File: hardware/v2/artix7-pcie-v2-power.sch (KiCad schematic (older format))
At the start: 45 parts, among them U3 LP5907MFX, X1 APXS006A0X4-SRZ, X2 APXS006A0X4-SRZ, X3 APXS006A0X4-SRZ, X4 APXS006A0X4-SRZ

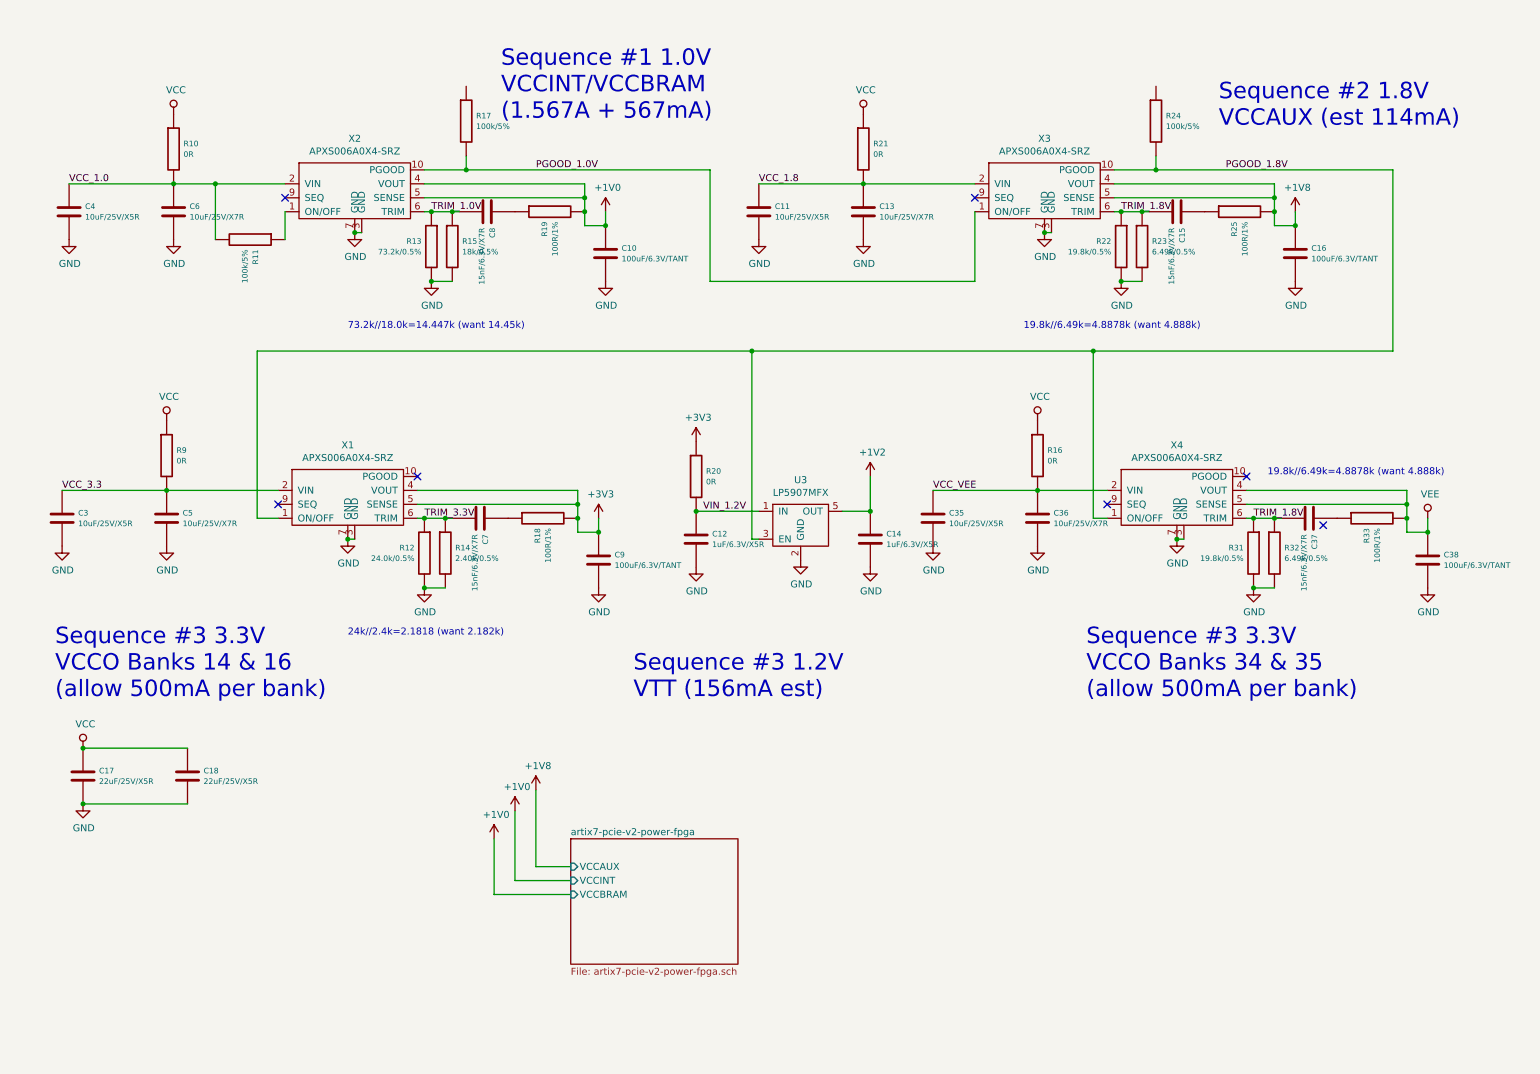
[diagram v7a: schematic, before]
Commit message: v2 pcb/schematic update : drc passing, need to add caps
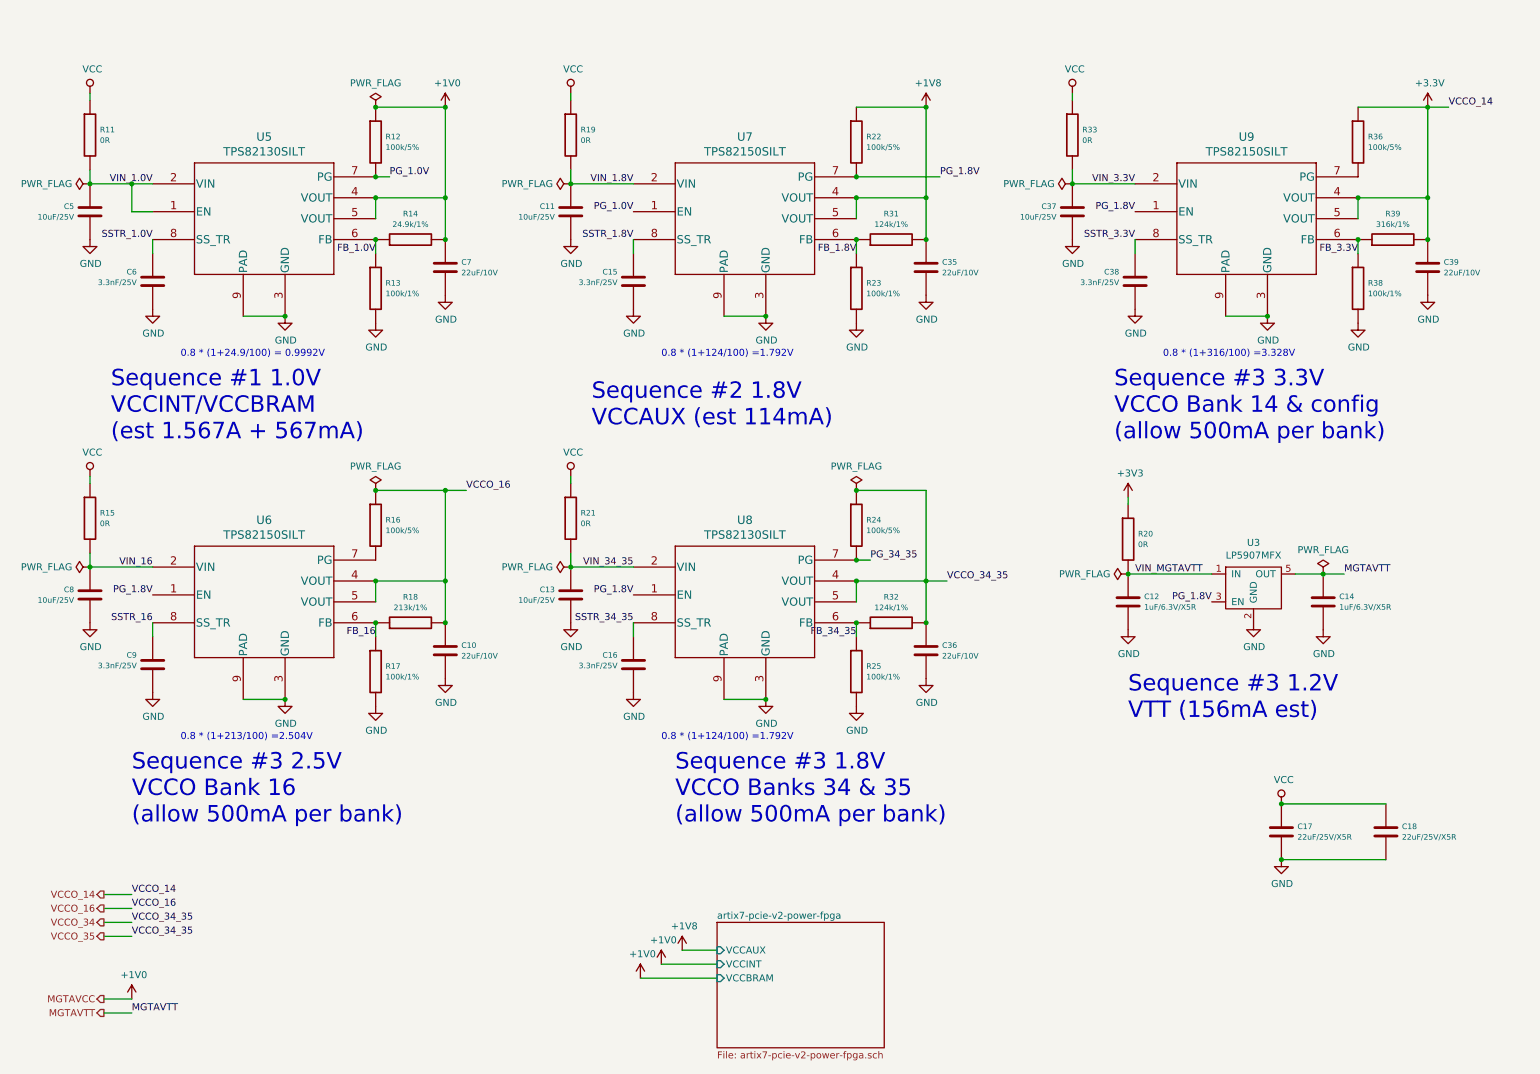
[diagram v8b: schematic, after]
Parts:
- removed C3, C4: 10uF/25V/X5R, tom-passives:C_0603_1608Metric_Pad1.05x0.95mm_HandSolder, symbol tom-passives:C
- removed R10, R9: 0R, tom-passives:C_0603_1608Metric, symbol tom-passives:R
- removed X1, X2, X3, X4: APXS006A0X4-SRZ, tom-modules:APXS006, symbol tom-modules:APXS006A0X4-SRZ
- added C39: 22uF/10V, tom-passives:C_0805_2012Metric, symbol tom-passives:C
- added R36: 100k/5%, tom-passives:C_0402_1005Metric, symbol tom-passives:R
- added R38: 100k/1%, tom-passives:C_0402_1005Metric, symbol tom-passives:R
- added R39: 316k/1%, tom-passives:C_0402_1005Metric, symbol tom-passives:R
- added U5, U8: TPS82130SILT, tom-modules:TPS82130SILT, symbol tom-modules:TPS821x0SILT
- added U6, U7, U9: TPS82150SILT, tom-modules:TPS82130SILT, symbol tom-modules:TPS821x0SILT
- C10: value 100uF/6.3V/TANT -> 22uF/10V; footprint tom-passives:C_0402_1005Metric -> tom-passives:C_0805_2012Metric; Digikey 478-9393-1-ND -> (none); MFGPN (none) -> C2012X7S1A226M125AC
- C11: value 10uF/25V/X5R -> 10uF/25V; footprint tom-passives:C_0603_1608Metric_Pad1.05x0.95mm_HandSolder -> tom-passives:C_1206_3216Metric; MFGPN (none) -> C3216X7R1E106M160AE
- C13, C5: value 10uF/25V/X7R -> 10uF/25V; footprint tom-passives:C_0603_1608Metric_Pad1.05x0.95mm_HandSolder -> tom-passives:C_1206_3216Metric; MFGPN (none) -> C3216X7R1E106M160AE
- C15: value 15nF/6.3V/X7R -> 3.3nF/25V
- C16, C38, C9: value 100uF/6.3V/TANT -> 3.3nF/25V; Digikey 478-9393-1-ND -> (none)
- C35: value 10uF/25V/X5R -> 22uF/10V; footprint tom-passives:C_0603_1608Metric_Pad1.05x0.95mm_HandSolder -> tom-passives:C_0805_2012Metric; MFGPN (none) -> C2012X7S1A226M125AC
- C36: value 10uF/25V/X7R -> 22uF/10V; footprint tom-passives:C_0603_1608Metric_Pad1.05x0.95mm_HandSolder -> tom-passives:C_0805_2012Metric; MFGPN (none) -> C2012X7S1A226M125AC
- C37, C8: value 15nF/6.3V/X7R -> 10uF/25V; footprint tom-passives:C_0402_1005Metric -> tom-passives:C_1206_3216Metric; MFGPN (none) -> C3216X7R1E106M160AE
- C6: value 10uF/25V/X7R -> 3.3nF/25V; footprint tom-passives:C_0603_1608Metric_Pad1.05x0.95mm_HandSolder -> tom-passives:C_0402_1005Metric
- C7: value 15nF/6.3V/X7R -> 22uF/10V; footprint tom-passives:C_0402_1005Metric -> tom-passives:C_0805_2012Metric; MFGPN (none) -> C2012X7S1A226M125AC
- R11: value 100k/5% -> 0R; footprint tom-passives:C_0402_1005Metric -> tom-passives:R_0603_1608Metric
- R12: value 24.0k/0.5% -> 100k/5%
- R13: value 73.2k/0.5% -> 100k/1%
- R14: value 2.40k/0.5% -> 24.9k/1%
- R15: value 18k/0.5% -> 0R; footprint tom-passives:C_0402_1005Metric -> tom-passives:R_0603_1608Metric
- R16: value 0R -> 100k/5%; footprint tom-passives:C_0603_1608Metric -> tom-passives:C_0402_1005Metric
- R17: value 100k/5% -> 100k/1%
- R18: value 100R/1% -> 213k/1%
- R19, R33: value 100R/1% -> 0R; footprint tom-passives:C_0402_1005Metric -> tom-passives:R_0603_1608Metric
- R21: footprint tom-passives:C_0402_1005Metric -> tom-passives:R_0603_1608Metric
- R22: value 19.8k/0.5% -> 100k/5%
- R23: value 6.49k/0.5% -> 100k/1%
- R25: value 100R/1% -> 100k/1%
- R31: value 19.8k/0.5% -> 124k/1%
- R32: value 6.49k/0.5% -> 124k/1%
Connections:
- net PGOOD_1.0V is gone; now on net GND: R17.2
- net VCC_3.3 is gone; now on net GND: C5.1
- net +1V0: now also C7.1, R12.1, R14.2, U5.4 (VOUT), U5.5 (VOUT); no longer C10.1, R19.2
- net +1V8: now also C35.1, R22.1, R31.2, U7.4 (VOUT), U7.5 (VOUT); no longer C16.1, R25.2
- net +3V3: now also C39.1, R36.1, R39.2, U9.4 (VOUT), U9.5 (VOUT); no longer C9.1, R18.2
- net GND: now also C11.1, C13.1, C15.1, C16.1, C37.1, C38.1, C6.1, C7.2, C8.1, C9.1, R25.2, C39.2, R38.2, U5.3 (GND), U5.9 (PAD), U6.3 (GND), U6.9 (PAD), U7.3 (GND), U7.9 (PAD), U8.3 (GND), U8.9 (PAD), U9.3 (GND), U9.9 (PAD); no longer C11.2, C13.2, C16.2, C38.2, C5.2, C6.2, C9.2, R12.2, R14.2, R15.2, R22.2, R31.2, R32.2
- net VCC: now also R11.1, R15.1, R19.1, R33.1; no longer R16.1
- net FB_16: now reaches R17.1
- net FB_16: now also R18.1, U6.6 (FB)
- net VCCO_34: now reaches R24.1
- net VCCO_34: now also C36.1, R32.2, U8.4 (VOUT), U8.5 (VOUT)
- net FB_34_35: now reaches R25.1
- net FB_34_35: now also R32.1, U8.6 (FB); no longer C15.1
- net +1V2 renamed MGTAVTT
- net PGOOD_1.8V renamed PG_1.8V
- net PG_1.8V: now also R22.2, U6.1 (EN), U7.7 (PG), U8.1 (EN), U9.1 (EN); no longer R24.2
- removed net TRIM_1.0V: C8.2, R13.1, R15.1
- removed net TRIM_1.8V: C15.2, C37.2, R22.1, R23.1, R31.1, R32.1
- removed net TRIM_3.3V: C7.2, R12.1, R14.1
- net VCC_1.0 renamed VIN_1.0V
- net VIN_1.0V: now also C5.2, U5.1 (EN), U5.2 (VIN); no longer C6.1
- removed net VCC_1.8: C11.1, C13.1, R21.2
- removed net VCC_VEE: C35.1, C36.1, R16.2
- net VEE renamed VIN_3.3V
- net VIN_3.3V: now also C37.2, U9.2 (VIN); no longer C38.1
- net VIN_1.2V renamed VIN_MGTAVTT
- new net: R36.2, U9.7 (PG)
- new net: R16.2, U6.7 (PG)
- new net FB_1.0V: R13.1, R14.1, U5.6 (FB)
- new net FB_1.8V: R23.1, R31.1, U7.6 (FB)
- new net FB_3.3V: R38.1, R39.1, U9.6 (FB)
- new net PG_1.0V: R12.2, U5.7 (PG), U7.1 (EN)
- new net PG_34_35: R24.2, U8.7 (PG)
- new net SSTR_1.0V: C6.2, U5.8 (SS_TR)
- new net SSTR_1.8V: C15.2, U7.8 (SS_TR)
- new net SSTR_16: C9.2, U6.8 (SS_TR)
- new net SSTR_3.3V: C38.2, U9.8 (SS_TR)
- new net SSTR_34_35: C16.2, U8.8 (SS_TR)
- new net VCCO_16: C10.1, R16.1, R18.2, U6.4 (VOUT), U6.5 (VOUT)
- new net VIN_1.8V: C11.2, R19.2, U7.2 (VIN)
- new net VIN_16: C8.2, R15.2, U6.2 (VIN)
- new net VIN_34_35: C13.2, R21.2, U8.2 (VIN)
- no-connect marks 7 -> 0
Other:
- note added: "0.8 * (1+124/100) =1.792V"
- note added: "0.8 * (1+213/100) =2.504V"
- note added: "0.8 * (1+24.9/100) = 0.9992V"
- note added: "0.8 * (1+316/100) =3.328V"
- note added: "Sequence #1 1.0V\nVCCINT/VCCBRAM\n(est 1.567A + 567mA)"
- note added: "Sequence #3 1.8V\nVCCO Banks 34 & 35\n(allow 500mA per bank)"
- note added: "Sequence #3 2.5V\nVCCO Bank 16\n(allow 500mA per bank)"
- note added: "Sequence #3 3.3V\nVCCO Bank 14 & config\n(allow 500mA per bank)"
- note removed: "19.8k//6.49k=4.8878k (want 4.888k)"
- note removed: "24k//2.4k=2.1818 (want 2.182k)"
- note removed: "73.2k//18.0k=14.447k (want 14.45k)"
- note removed: "Sequence #1 1.0V\nVCCINT/VCCBRAM\n(1.567A + 567mA)"
- note removed: "Sequence #3 3.3V\nVCCO Banks 14 & 16\n(allow 500mA per bank)"
- note removed: "Sequence #3 3.3V\nVCCO Banks 34 & 35\n(allow 500mA per bank)"
- moved on the sheet: C12, C14, C17, C18, R20, U3
